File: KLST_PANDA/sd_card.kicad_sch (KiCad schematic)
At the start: 8 parts, among them J1 Micro_SD_Card_Det_Hirose_DM3AT

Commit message: cleaned up
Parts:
- renumbered R11 to R13, R12 to R14, R13 to R15, R14 to R16, R15 to R17
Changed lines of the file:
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@@
         )
         (path "/b4513875-4c57-4720-bcc5-43ead67fe18f/52cda7d1-da0e-43fc-963f-d09ac6e0ff74"
-          (reference "#PWR040") (unit 1)
+          (reference "#PWR041") (unit 1)
         )
       )
@@
         )
         (path "/b4513875-4c57-4720-bcc5-43ead67fe18f/52cda7d1-da0e-43fc-963f-d09ac6e0ff74"
-          (reference "#PWR039") (unit 1)
+          (reference "#PWR040") (unit 1)
         )
       )
@@
         )
         (path "/b4513875-4c57-4720-bcc5-43ead67fe18f/52cda7d1-da0e-43fc-963f-d09ac6e0ff74"
-          (reference "#PWR038") (unit 1)
+          (reference "#PWR039") (unit 1)
         )
       )
@@
         )
         (path "/b4513875-4c57-4720-bcc5-43ead67fe18f/52cda7d1-da0e-43fc-963f-d09ac6e0ff74"
-          (reference "#PWR041") (unit 1)
+          (reference "#PWR042") (unit 1)
         )
       )
@@
   (symbol (lib_id "Device:R_Small") (at 121.285 33.655 0) (unit 1)
     (in_bom yes) (on_board yes) (dnp no) (fields_autoplaced)
-    (property "Reference" "R15" (at 123.19 33.02 0)
+    (property "Reference" "R17" (at 123.19 33.02 0)
       (effects (font (size 1.27 1.27)) (justify left))
     )
@@
       (project "KLST_PANDA"
         (path "/b4513875-4c57-4720-bcc5-43ead67fe18f/52cda7d1-da0e-43fc-963f-d09ac6e0ff74"
+          (reference "R17") (unit 1)
+        )
+      )
+    )
+  )
+  (symbol (lib_id "Device:R_Small") (at 113.665 33.655 0) (unit 1)
+    (in_bom yes) (on_board yes) (dnp no) (fields_autoplaced)
+    (property "Reference" "R16" (at 115.57 33.02 0)
+      (effects (font (size 1.27 1.27)) (justify left))
+    )
+    (property "Value" "47K" (at 115.57 35.56 0)
+      (effects (font (size 1.27 1.27)) (justify left))
+    )
+    (property "Footprint" "" (at 113.665 33.655 0)
+      (effects (font (size 1.27 1.27)) hide)
+    )
+    (property "Datasheet" "~" (at 113.665 33.655 0)
+      (effects (font (size 1.27 1.27)) hide)
+    )
+    (pin "1")
+    (pin "2")
+    (instances
+      (project "KLST_PANDA"
+        (path "/b4513875-4c57-4720-bcc5-43ead67fe18f/52cda7d1-da0e-43fc-963f-d09ac6e0ff74"
+          (reference "R16") (unit 1)
+        )
+      )
+    )
+  )
+  (symbol (lib_id "Device:R_Small") (at 106.045 33.655 0) (unit 1)
+    (in_bom yes) (on_board yes) (dnp no) (fields_autoplaced)
+    (property "Reference" "R15" (at 107.95 33.02 0)
+      (effects (font (size 1.27 1.27)) (justify left))
+    )
+    (property "Value" "47K" (at 107.95 35.56 0)
+      (effects (font (size 1.27 1.27)) (justify left))
+    )
+    (property "Footprint" "" (at 106.045 33.655 0)
+      (effects (font (size 1.27 1.27)) hide)
+    )
+    (property "Datasheet" "~" (at 106.045 33.655 0)
+      (effects (font (size 1.27 1.27)) hide)
+    )
+    (pin "1")
+    (pin "2")
+    (instances
+      (project "KLST_PANDA"
+        (path "/b4513875-4c57-4720-bcc5-43ead67fe18f/52cda7d1-da0e-43fc-963f-d09ac6e0ff74"
           (reference "R15") (unit 1)
-        )
-      )
-    )
-  )
-  (symbol (lib_id "Device:R_Small") (at 113.665 33.655 0) (unit 1)
-    (in_bom yes) (on_board yes) (dnp no) (fields_autoplaced)
-    (property "Reference" "R14" (at 115.57 33.02 0)
-      (effects (font (size 1.27 1.27)) (justify left))
-    )
-    (property "Value" "47K" (at 115.57 35.56 0)
-      (effects (font (size 1.27 1.27)) (justify left))
-    )
-    (property "Footprint" "" (at 113.665 33.655 0)
-      (effects (font (size 1.27 1.27)) hide)
-    )
-    (property "Datasheet" "~" (at 113.665 33.655 0)
-      (effects (font (size 1.27 1.27)) hide)
-    )
-    (pin "1")
-    (pin "2")
-    (instances
-      (project "KLST_PANDA"
-        (path "/b4513875-4c57-4720-bcc5-43ead67fe18f/52cda7d1-da0e-43fc-963f-d09ac6e0ff74"
-          (reference "R14") (unit 1)
-        )
-      )
-    )
-  )
-  (symbol (lib_id "Device:R_Small") (at 106.045 33.655 0) (unit 1)
-    (in_bom yes) (on_board yes) (dnp no) (fields_autoplaced)
-    (property "Reference" "R13" (at 107.95 33.02 0)
-      (effects (font (size 1.27 1.27)) (justify left))
-    )
-    (property "Value" "47K" (at 107.95 35.56 0)
-      (effects (font (size 1.27 1.27)) (justify left))
-    )
-    (property "Footprint" "" (at 106.045 33.655 0)
-      (effects (font (size 1.27 1.27)) hide)
-    )
-    (property "Datasheet" "~" (at 106.045 33.655 0)
-      (effects (font (size 1.27 1.27)) hide)
-    )
-    (pin "1")
-    (pin "2")
-    (instances
-      (project "KLST_PANDA"
-        (path "/b4513875-4c57-4720-bcc5-43ead67fe18f/52cda7d1-da0e-43fc-963f-d09ac6e0ff74"
-          (reference "R13") (unit 1)
         )
       )
@@
   (symbol (lib_id "Device:R_Small") (at 90.805 33.655 0) (unit 1)
     (in_bom yes) (on_board yes) (dnp no) (fields_autoplaced)
-    (property "Reference" "R11" (at 92.71 33.02 0)
+    (property "Reference" "R13" (at 92.71 33.02 0)
       (effects (font (size 1.27 1.27)) (justify left))
     )
@@
       (project "KLST_PANDA"
         (path "/b4513875-4c57-4720-bcc5-43ead67fe18f/52cda7d1-da0e-43fc-963f-d09ac6e0ff74"
-          (reference "R11") (unit 1)
+          (reference "R13") (unit 1)
         )
       )
@@
   (symbol (lib_id "Device:R_Small") (at 98.425 33.655 0) (unit 1)
     (in_bom yes) (on_board yes) (dnp no) (fields_autoplaced)
-    (property "Reference" "R12" (at 100.33 33.02 0)
+    (property "Reference" "R14" (at 100.33 33.02 0)
       (effects (font (size 1.27 1.27)) (justify left))
     )
@@
       (project "KLST_PANDA"
         (path "/b4513875-4c57-4720-bcc5-43ead67fe18f/52cda7d1-da0e-43fc-963f-d09ac6e0ff74"
-          (reference "R12") (unit 1)
+          (reference "R14") (unit 1)
         )
       )
@@
         )
         (path "/b4513875-4c57-4720-bcc5-43ead67fe18f/52cda7d1-da0e-43fc-963f-d09ac6e0ff74"
-          (reference "R10") (unit 1)
-        )
-      )
+          (reference "R12") (unit 1)
+        )
+      )

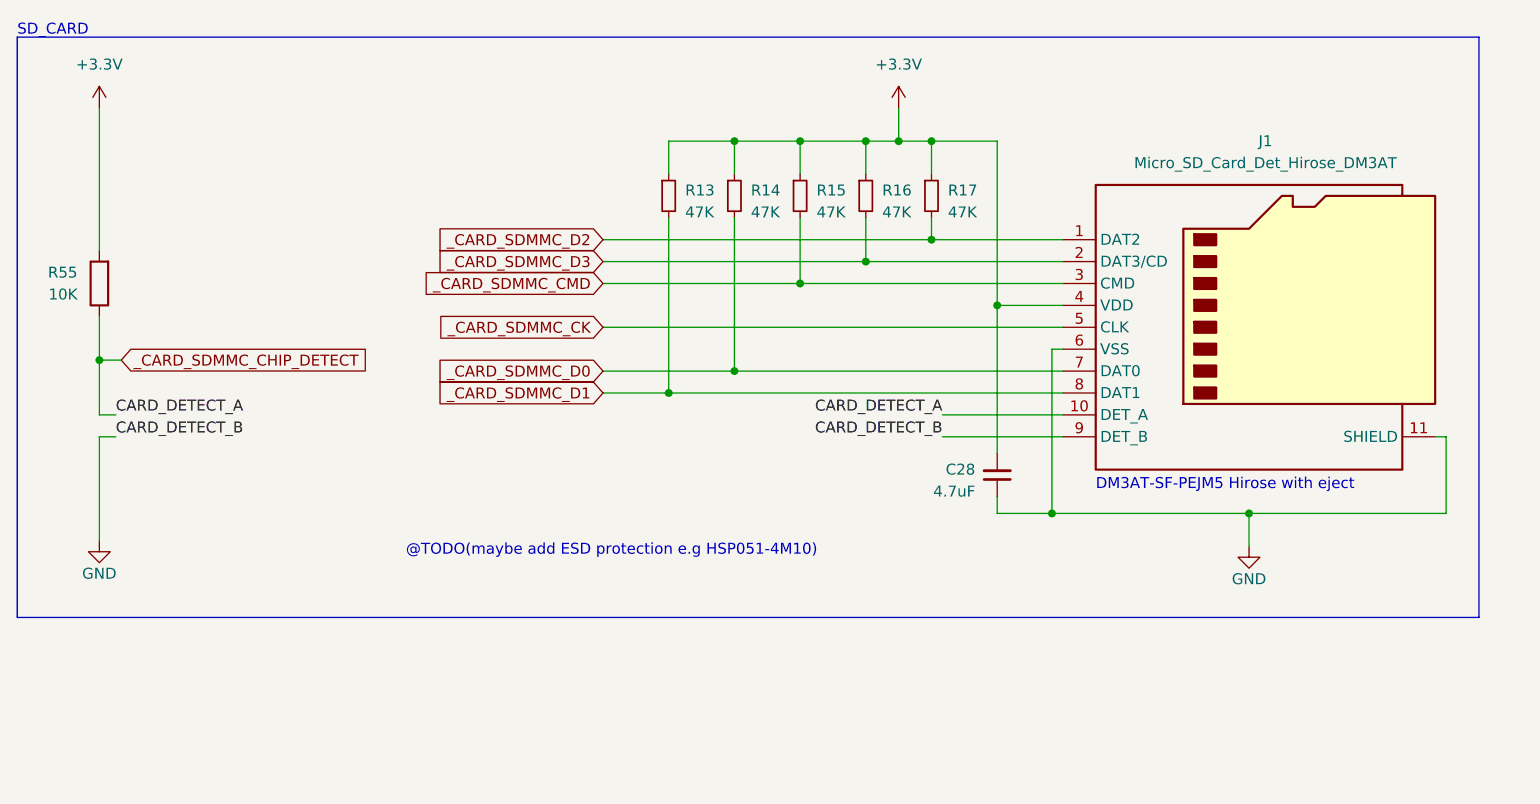
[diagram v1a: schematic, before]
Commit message: unified internal I2C bus, cleaned up, added ESD protection to USB
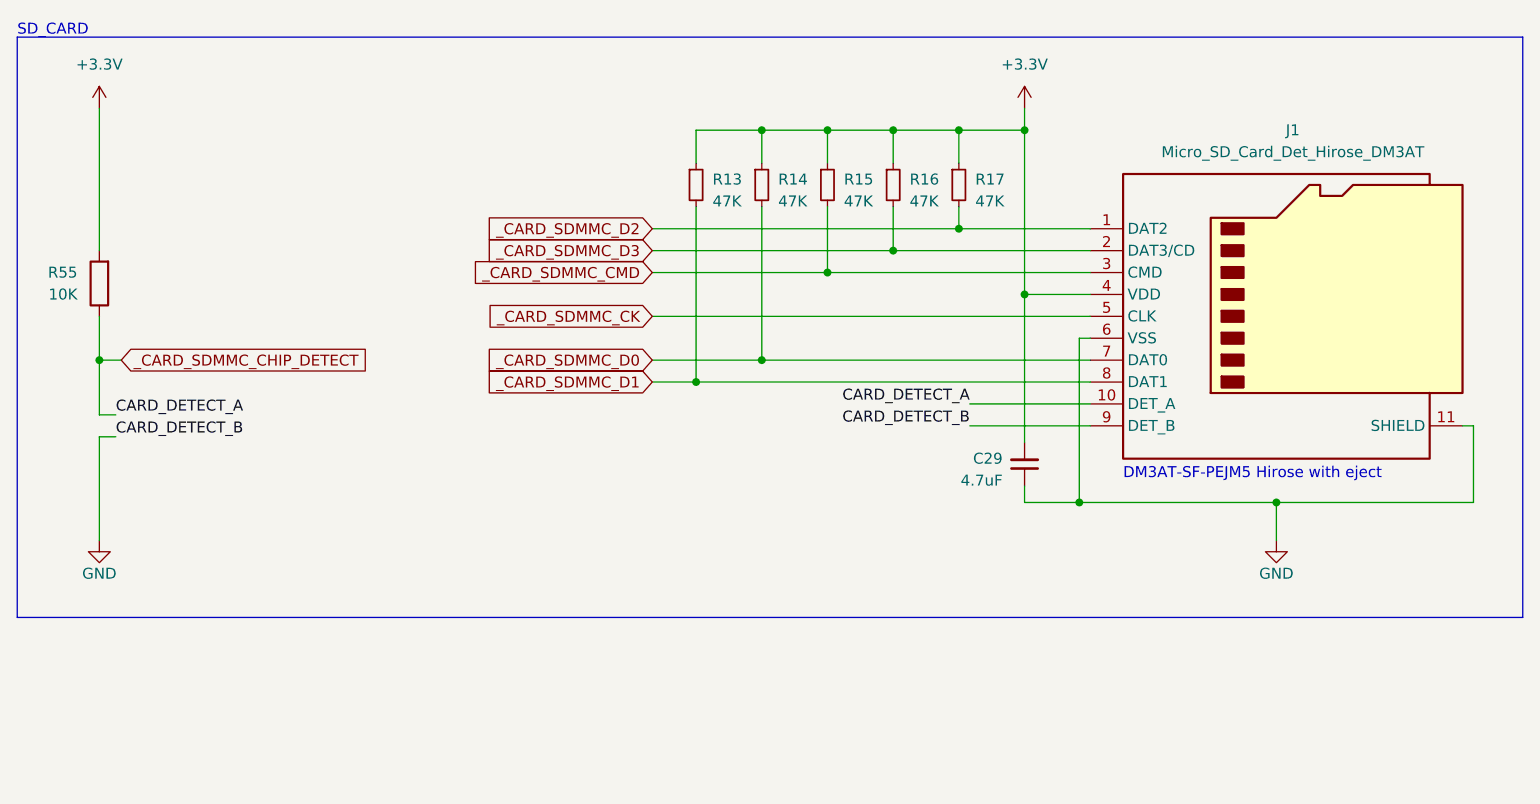
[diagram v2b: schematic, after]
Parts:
- renumbered C28 to C29
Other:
- note removed: "@TODO(maybe add ESD protection e.g HSP051-4M10)"
- moved on the sheet: C29, J1, R13, R14, R15, R16, R17

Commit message: started spec'ing components
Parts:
- C29: footprint (none) -> Capacitor_SMD:C_0402_1005Metric; JLCPCB (none) -> C23733
- R13, R14, R15, R16, R17: footprint (none) -> Resistor_SMD:R_0402_1005Metric; JLCPCB (none) -> C25563
- R55: JLCPCB (none) -> C25744; JLCPCB Part # C25744 -> (none)
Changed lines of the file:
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@@
       (effects (font (size 1.27 1.27)) (justify left))
     )
-    (property "Footprint" "" (at 124.46 32.385 0)
+    (property "Footprint" "Resistor_SMD:R_0402_1005Metric" (at 124.46 32.385 0)
       (effects (font (size 1.27 1.27)) hide)
     )
@@
       (effects (font (size 1.27 1.27)) hide)
     )
+    (property "JLCPCB" "C25563" (at 124.46 32.385 0)
+      (effects (font (size 1.27 1.27)) hide)
+    )
     (pin "1")
     (pin "2")
@@
       (effects (font (size 1.27 1.27)) (justify left))
     )
-    (property "Footprint" "" (at 116.84 32.385 0)
+    (property "Footprint" "Resistor_SMD:R_0402_1005Metric" (at 116.84 32.385 0)
       (effects (font (size 1.27 1.27)) hide)
     )
@@
       (effects (font (size 1.27 1.27)) hide)
     )
+    (property "JLCPCB" "C25563" (at 116.84 32.385 0)
+      (effects (font (size 1.27 1.27)) hide)
+    )
     (pin "1")
     (pin "2")
@@
       (effects (font (size 1.27 1.27)) (justify left))
     )
-    (property "Footprint" "" (at 109.22 32.385 0)
+    (property "Footprint" "Resistor_SMD:R_0402_1005Metric" (at 109.22 32.385 0)
       (effects (font (size 1.27 1.27)) hide)
     )
     (property "Datasheet" "~" (at 109.22 32.385 0)
+      (effects (font (size 1.27 1.27)) hide)
+    )
+    (property "JLCPCB" "C25563" (at 109.22 32.385 0)
       (effects (font (size 1.27 1.27)) hide)
     )
@@
       (effects (font (size 1.27 1.27)) (justify left))
     )
-    (property "Footprint" "" (at 93.98 32.385 0)
+    (property "Footprint" "Resistor_SMD:R_0402_1005Metric" (at 93.98 32.385 0)
       (effects (font (size 1.27 1.27)) hide)
     )
     (property "Datasheet" "~" (at 93.98 32.385 0)
+      (effects (font (size 1.27 1.27)) hide)
+    )
+    (property "JLCPCB" "C25563" (at 93.98 32.385 0)
       (effects (font (size 1.27 1.27)) hide)
     )
@@
       (effects (font (size 1.27 1.27)) (justify right))
     )
-    (property "Footprint" "" (at 132.08 64.77 0)
+    (property "Footprint" "Capacitor_SMD:C_0402_1005Metric" (at 132.08 64.77 0)
       (effects (font (size 1.27 1.27)) hide)
     )
@@
       (effects (font (size 1.27 1.27)) hide)
     )
+    (property "Description" "10V" (at 132.08 64.77 0)
+      (effects (font (size 1.27 1.27)) hide)
+    )
+    (property "JLCPCB" "C23733" (at 132.08 64.77 0)
+      (effects (font (size 1.27 1.27)) hide)
+    )
     (pin "1")
     (pin "2")
@@
       (effects (font (size 1.27 1.27)) (justify left))
     )
-    (property "Footprint" "" (at 101.6 32.385 0)
+    (property "Footprint" "Resistor_SMD:R_0402_1005Metric" (at 101.6 32.385 0)
       (effects (font (size 1.27 1.27)) hide)
     )
     (property "Datasheet" "~" (at 101.6 32.385 0)
+      (effects (font (size 1.27 1.27)) hide)
+    )
+    (property "JLCPCB" "C25563" (at 101.6 32.385 0)
       (effects (font (size 1.27 1.27)) hide)
     )
@@
       (effects (font (size 1.27 1.27)) hide)
     )
-    (property "JLCPCB Part #" "C25744" (at 24.765 43.815 0)
-      (effects (font (size 1.27 1.27)) hide)
-    )
+    (property "JLCPCB Part #" "" (at 24.765 43.815 0)
+      (effects (font (size 1.27 1.27)) hide)
+    )
+    (property "JLCPCB" "C25744" (at 24.765 43.815 0)
+      (effects (font (size 1.27 1.27)) hide)
+    )

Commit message: cleaned up footprint assignment
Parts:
- R55: Extended Part - -> (none); MFR.Part # 0402WGF1002TCE -> (none)
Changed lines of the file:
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@@
-      (effects (font (size 1.27 1.27)) hide)
-    )
-    (property "MFR.Part #" "0402WGF1002TCE" (at 24.765 43.815 0)
-      (effects (font (size 1.27 1.27)) hide)
-    )
-    (property "LCSC Part #" "" (at 24.765 43.815 0)
-      (effects (font (size 1.27 1.27)) hide)
-    )
-    (property "Extended Part" "-" (at 24.765 43.815 0)
-      (effects (font (size 1.27 1.27)) hide)
-    )
-    (property "JLCPCB Part #" "" (at 24.765 43.815 0)
       (effects (font (size 1.27 1.27)) hide)
     )

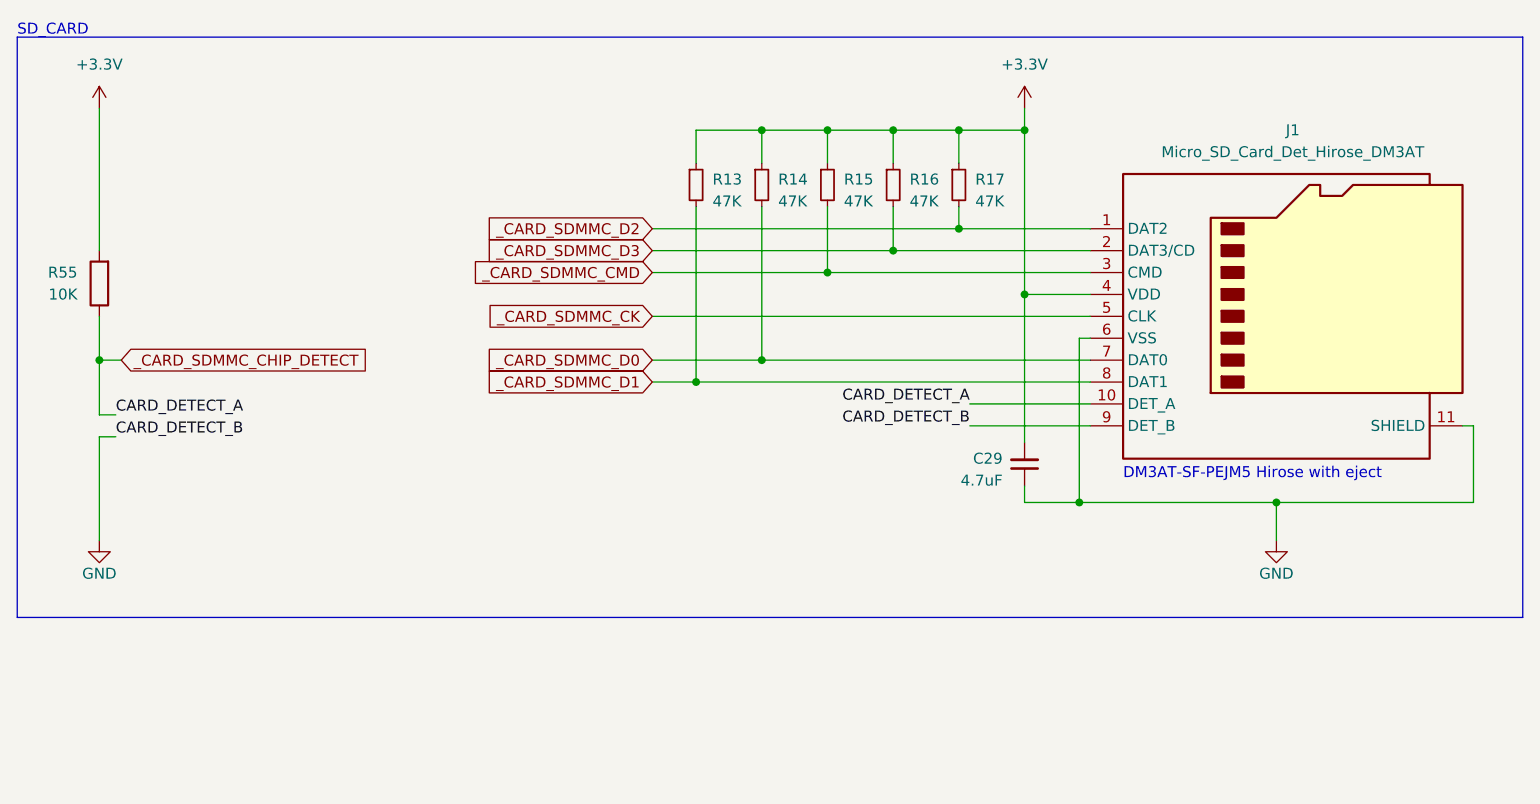
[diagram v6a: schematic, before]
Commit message: added resistor and capacitor, cleaned up TODOs
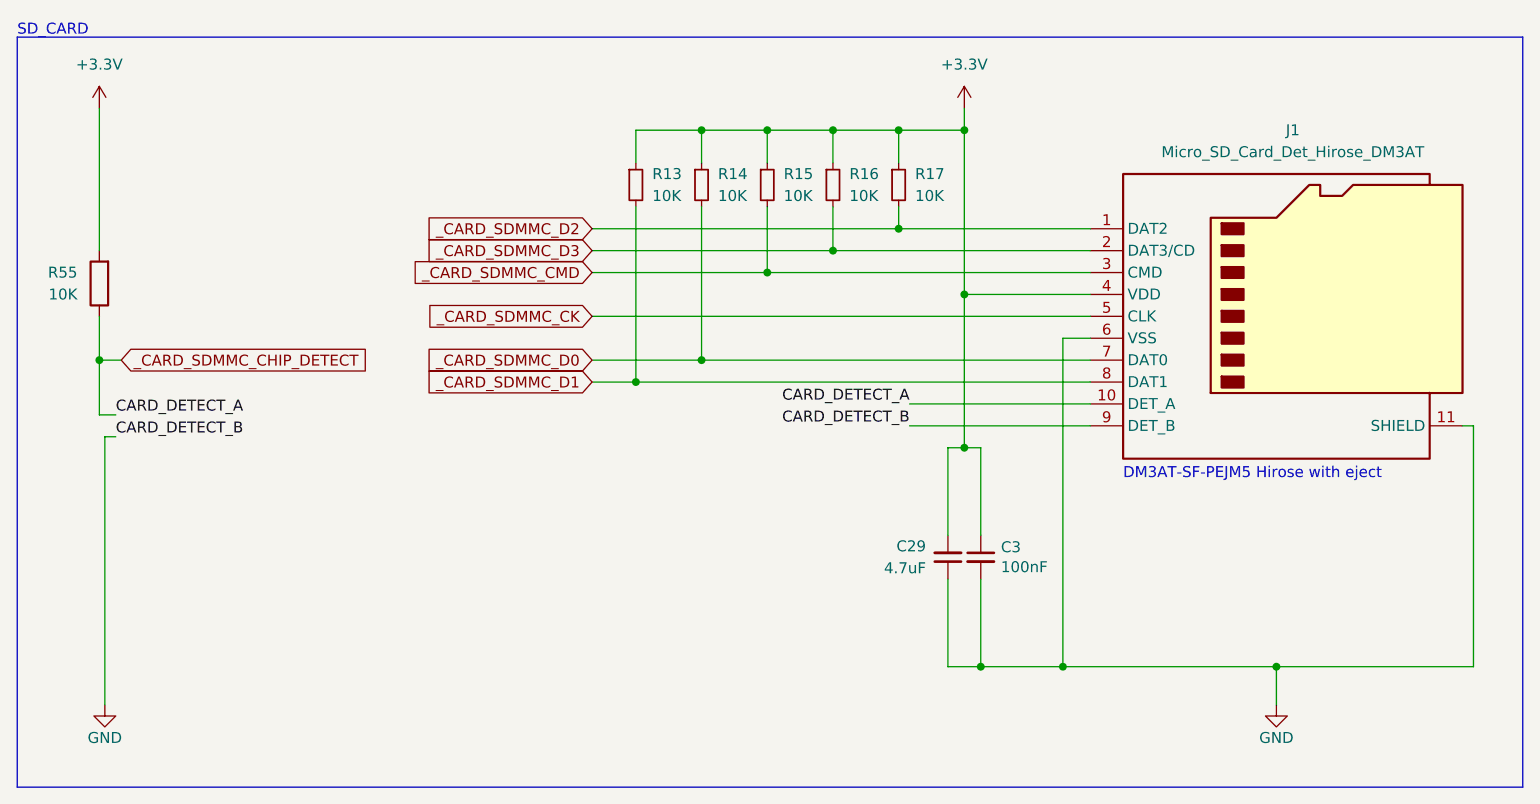
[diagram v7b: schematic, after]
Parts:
- added C3: 100nF, Capacitor_SMD:C_0402_1005Metric, symbol Device:C_Small
- R13, R14, R15, R16, R17: value 47K -> 10K; JLCPCB C25563 -> C25744
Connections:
- net +3.3V: now also C3.1
- net GND: now also C3.2
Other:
- moved on the sheet: C29, R13, R14, R15, R16, R17
